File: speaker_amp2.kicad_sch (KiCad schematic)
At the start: 24 parts, among them U1 TAS5822MDCPR

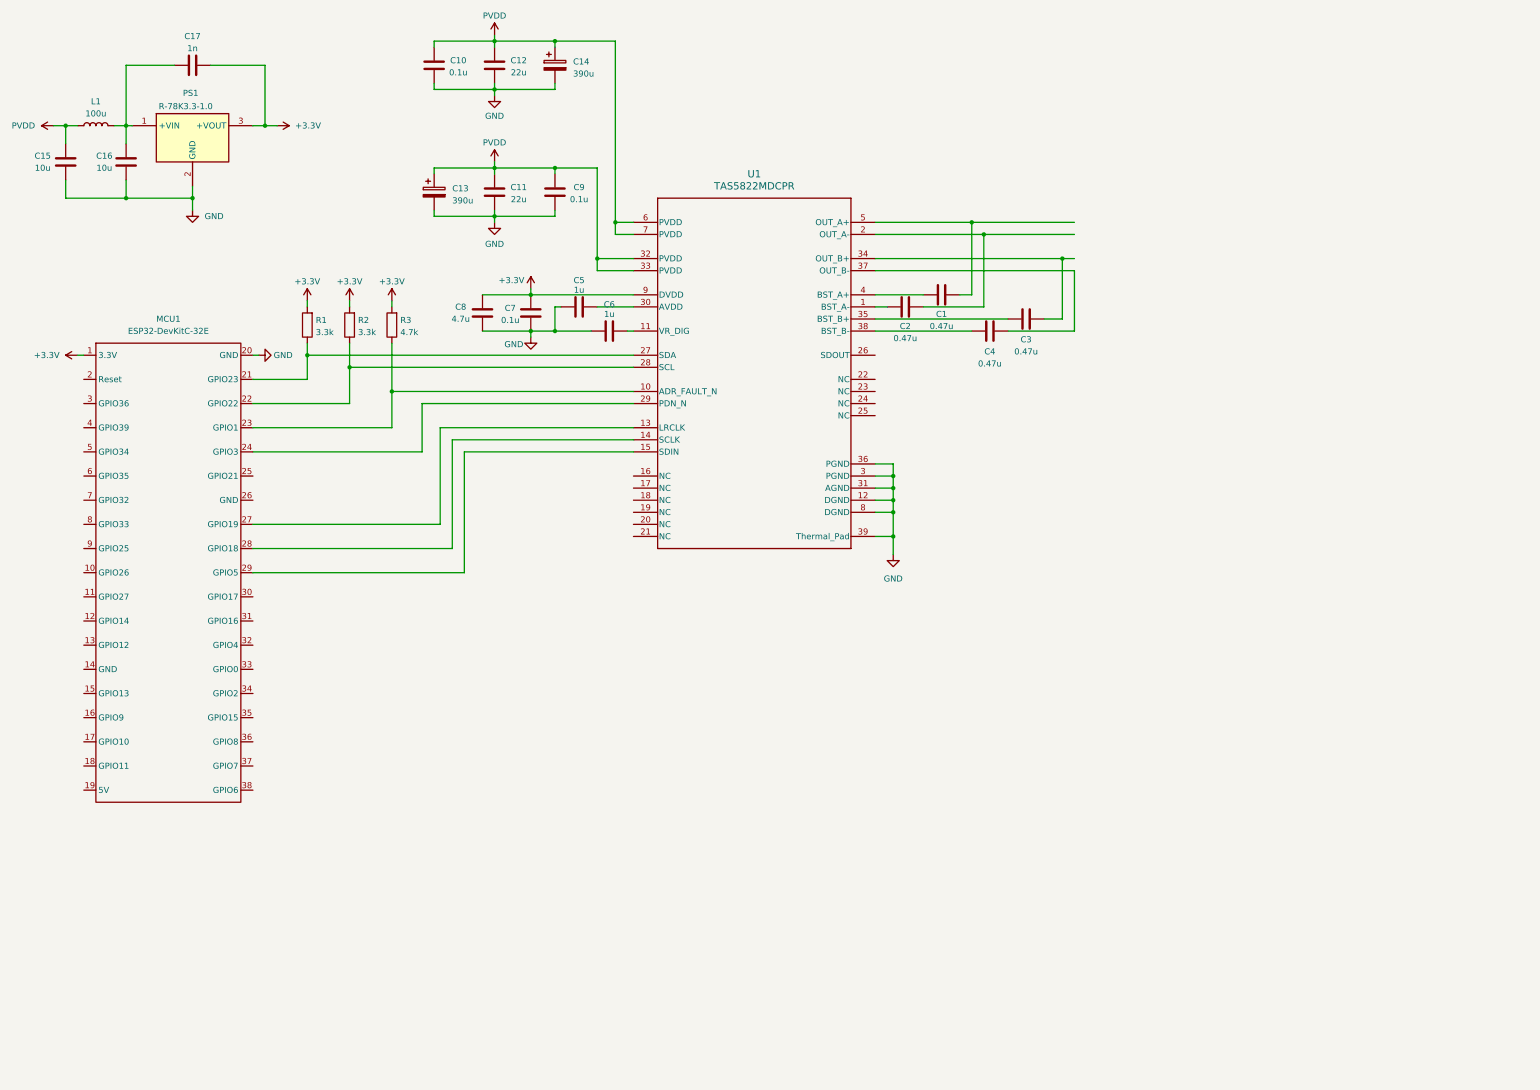
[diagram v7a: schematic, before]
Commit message: added C_BTL capacitor
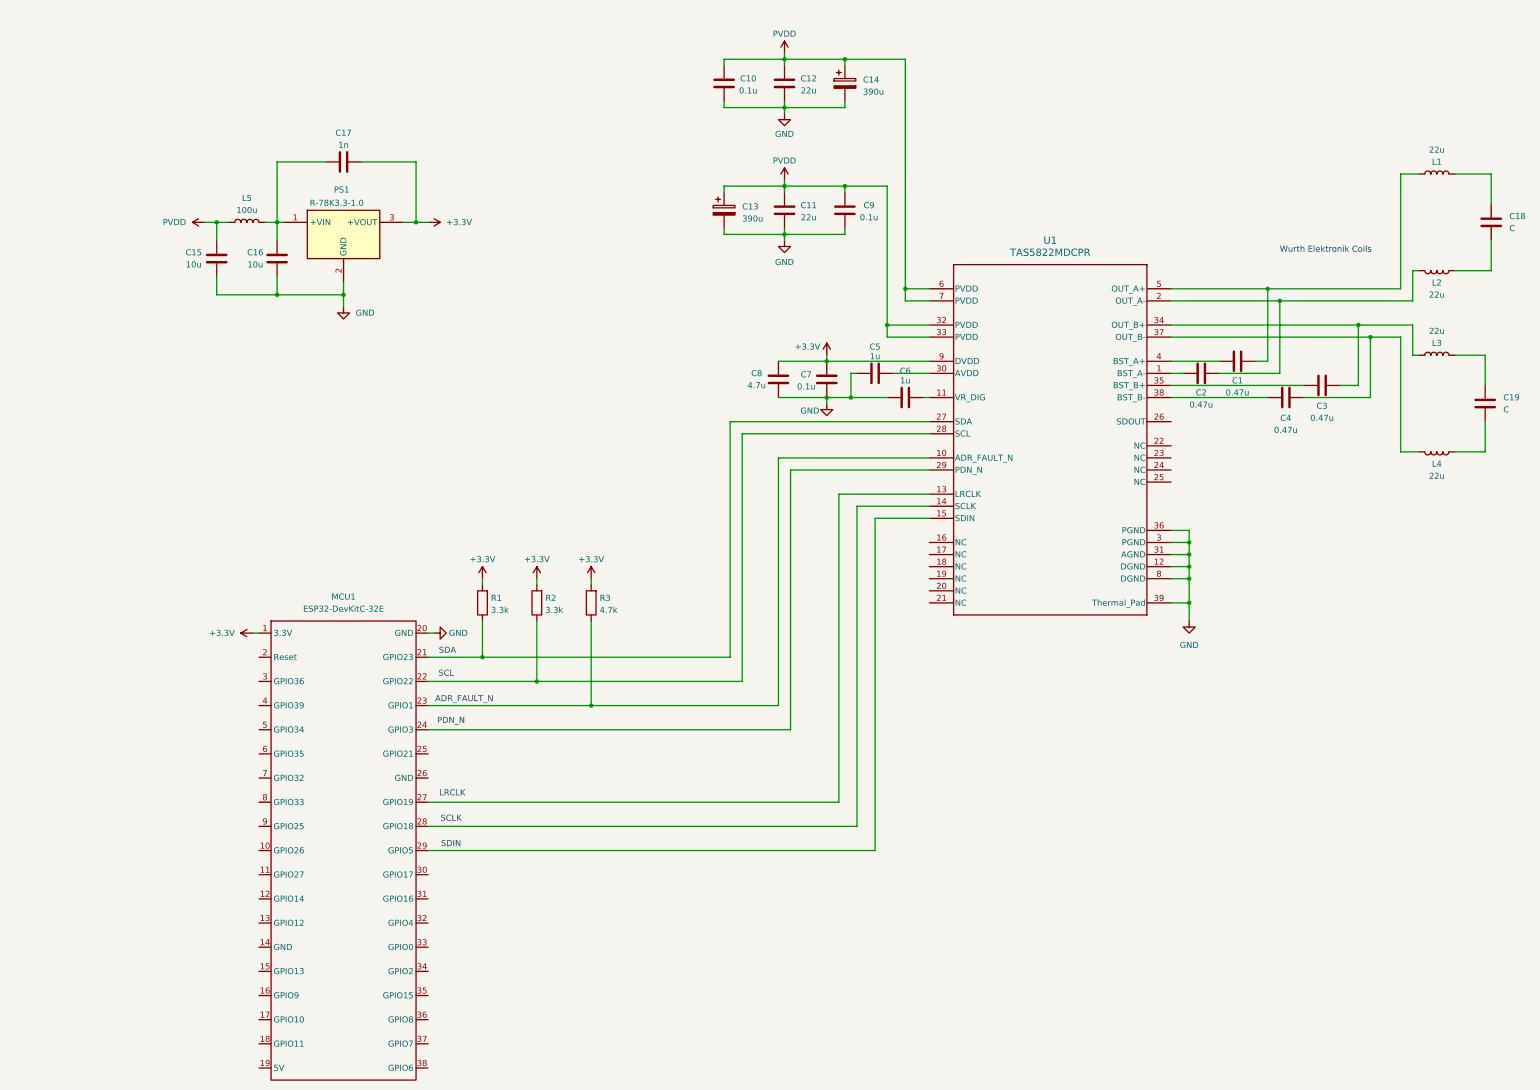
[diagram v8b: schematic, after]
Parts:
- added C18, C19: C, Capacitor_THT:C_Rect_L18.0mm_W9.0mm_P15.00mm_FKS3_FKP3, symbol Device:C
- added L1, L2, L3, L4: 22u, Inductor_SMD:L_Wuerth_WE-PD-Typ-LS_Handsoldering, symbol Device:L
- renumbered L1 to L5
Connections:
- net at C1.2, U1.5 (OUT_A+): now also L1.1
- net at C2.2, U1.2 (OUT_A-): now also L2.2
- net at C3.2, U1.34 (OUT_B+): now also L3.1
- net at C4.2, U1.37 (OUT_B-): now also L4.2
- new net: C18.2, L2.1
- new net: C18.1, L1.2
- new net: C19.2, L4.1
- new net: C19.1, L3.2
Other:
- note added: "ADR_FAULT_N"
- note added: "LRCLK"
- note added: "PDN_N"
- note added: "SCL"
- note added: "SCLK"
- note added: "SDA"
- note added: "SDIN"
- note added: "Wurth Elektronik Coils"
- moved on the sheet: C1, C10, C11, C12, C13, C14, C15, C16, C17, C2, C3, C4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
